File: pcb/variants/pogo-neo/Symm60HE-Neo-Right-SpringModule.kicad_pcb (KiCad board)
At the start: 2 copper layers, 20 x 6 mm, 2 parts

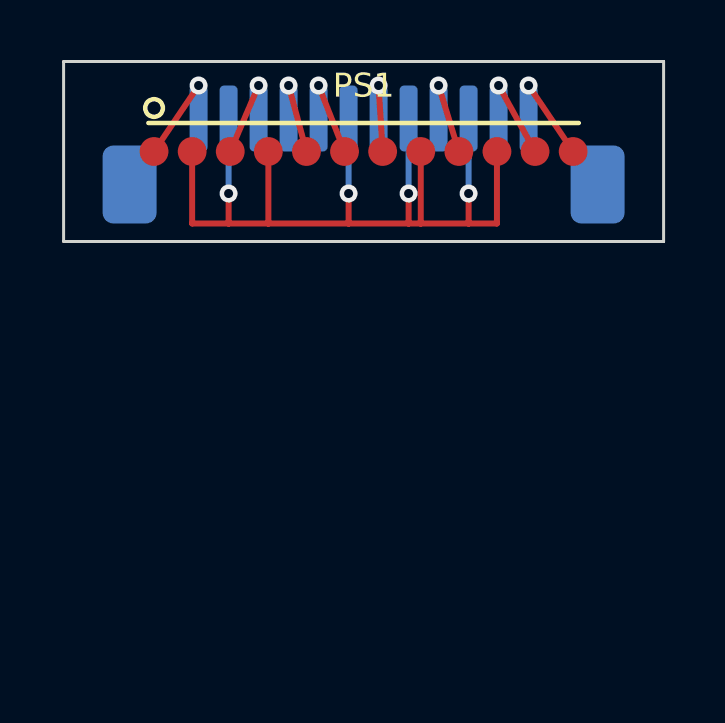
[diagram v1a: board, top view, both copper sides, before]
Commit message: Replace the project with the reorganised T7 tree: ribbon keyboard is production, pogo archived
Production design is now the outward-facing FPC keyboard with per-key
SK6812MINI-E reverse-mount LEDs, a fifth SN74LV4051A mux per half so every
alternate Hall position has its own channel, an SN74AHCT1G125 LED level
shifter, a 50 x 31 mm daughterboard, 1.5 mm POM plates and 3 degree / 7 degree
tent and typing angles. The universal half panel is fully populated (359
placements) with routed NPTH alignment slots for the mutually exclusive
positions, and eight fixed-layout Left/Right PCB pairs are released under
release/layout-pcbs/ with matching BOM, CPL, Gerber ZIP, drill report and DRC.

Reorganise tools/ into cad/, generators/, layouts/, pcb/, pogo/, releases/ and
rendering/ subpackages; add designs/ and layout/ (KLE) trees and per-layout
gallery renders. The Fusion handoff is a fourteen-body reference STEP with
Gateron KS-20 switch and Cherry-profile keycap references and exact BOOMELE,
HRO and XKB models under case/fusion360/models/official/ with provenance.

The Neo-style pogo variant, its Mill-Max vendor models, the Fusion setup
script and the pogo release packages are archived as design history and
marked DO-NOT-ORDER. Their restored BOM snapshots had reintroduced the wrong
mux part C7792; corrected to C128414 / SN74LV4051ADR and their checksum lists
and archives rebuilt.

Co-Authored-By: Claude Opus 5 <noreply@anthropic.com>
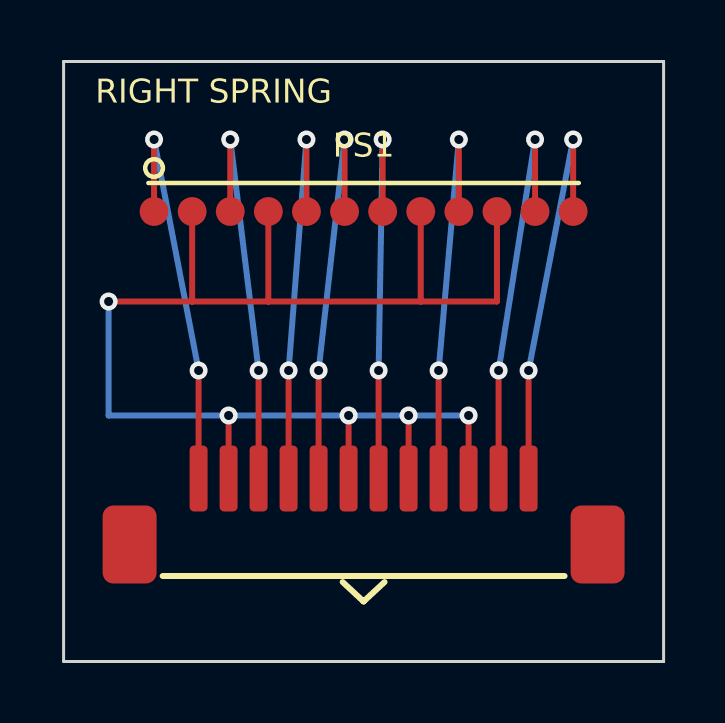
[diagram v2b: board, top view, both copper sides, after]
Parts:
- JF1: moved to F.Cu
- moved JF1 12.0 mm to (10.0, 15.0)
- moved PS1 2.00 mm to (10.0, 5.00)
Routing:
- net GND: track 33.8 -> 49.1 mm, vias 4 -> 5
- net ADC_R1: track 3.30 -> 13.7 mm, vias 1 -> 2
- net MUX_A1: track 3.38 -> 13.7 mm, vias 1 -> 2
- net ADC_R2: track 3.40 -> 13.7 mm, vias 1 -> 2
- net MUX_A2: track 3.46 -> 13.7 mm, vias 1 -> 2
- net MUX_A0: track 3.49 -> 13.8 mm, vias 1 -> 2
- net ADC_R3: track 3.61 -> 13.8 mm, vias 1 -> 2
- net ADC_R4: track 3.75 -> 13.8 mm, vias 1 -> 2
- net +3V3A: track 3.75 -> 13.8 mm, vias 1 -> 2
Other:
- board size 20 x 6 mm -> 20 x 20 mm
- board text added: "RIGHT SPRING"

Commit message: Neo-pogo: 3 deg tent, 7 deg typing, 20 x 6 mm spring heads; integrated Fusion reference
Regenerate the five Neo boards, both family panels, and the JLCPCB and
PCBWay release packages for the narrower floating spring heads and the
controller mounted left-to-right under the centre blocker. Rebuild the Fusion
reference set around a single integrated master STEP
(Symm60HE-case-reference-assembly.step) and rewrite the Fusion setup script
to import it as one grounded assembly.

Strip macOS AppleDouble (._*) files that a Mac copy introduced: they had been
swept into every PCBWay Gerber ZIP, both release archives and the SHA256SUMS
lists. Rebuild those archives and checksums, make both release generators skip
._* and .DS_Store, and ignore ._* and .recovery/ in git.

Co-Authored-By: Claude Opus 5 <noreply@anthropic.com>
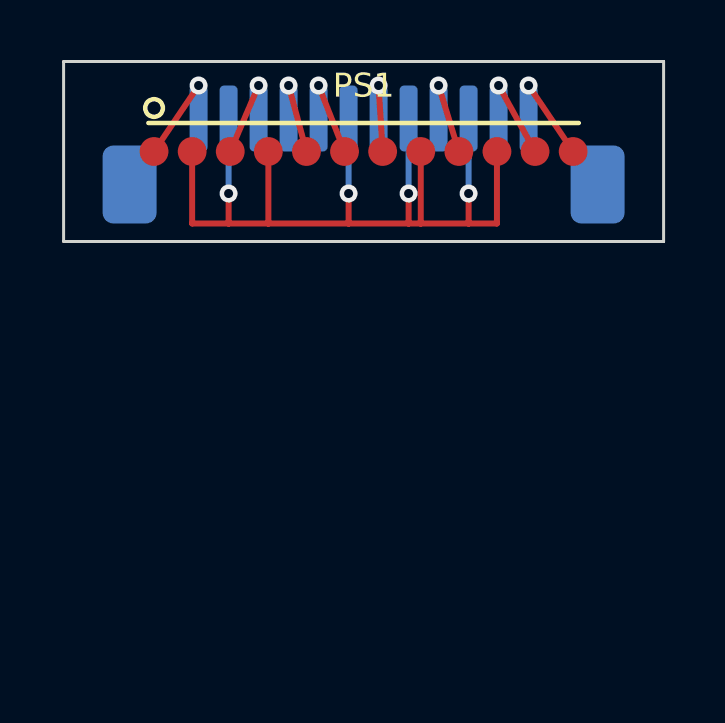
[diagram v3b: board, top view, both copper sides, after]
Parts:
- JF1: moved to B.Cu
- moved JF1 12.0 mm to (10.0, 3.00)
- moved PS1 2.00 mm to (10.0, 3.00)
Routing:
- net GND: track 49.1 -> 33.8 mm, vias 5 -> 4
- net ADC_R1: track 13.7 -> 3.30 mm, vias 2 -> 1
- net MUX_A1: track 13.7 -> 3.38 mm, vias 2 -> 1
- net ADC_R2: track 13.7 -> 3.40 mm, vias 2 -> 1
- net MUX_A2: track 13.7 -> 3.46 mm, vias 2 -> 1
- net MUX_A0: track 13.8 -> 3.49 mm, vias 2 -> 1
- net ADC_R3: track 13.8 -> 3.61 mm, vias 2 -> 1
- net ADC_R4: track 13.8 -> 3.75 mm, vias 2 -> 1
- net +3V3A: track 13.8 -> 3.75 mm, vias 2 -> 1
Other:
- board size 20 x 20 mm -> 20 x 6 mm
- board text removed: "RIGHT SPRING"
